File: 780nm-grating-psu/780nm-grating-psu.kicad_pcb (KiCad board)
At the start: 2 copper layers, 92.1 x 48.3 mm, 104 parts, among them IC1 ADP7142ARDZ-5.0-R7, IC2 LT8618EDDB#TRPBF, J1 TSW-102-07-G-D, J2 1755736, J3 54-00166, J4 TSW-102-07-G-S, J7 1715747, Q1 FDD3N40TM, Q2 2N7002, Q3 2N7002, U1 LT3757AEDD, U2 ADP7142ARDZ-3.3

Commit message: finished part placement
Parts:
- added REF**: Symbol_HighVoltage_Triangle_6x6mm_Copper, Symbol:Symbol_HighVoltage_Triangle_6x6mm_Copper, F.Cu at (191.0, 55.3)
- added SYM: Caution_Hot_Surface_FinalFit_12x12mm_Silk, caution:Caution_Hot_Surface_FinalFit_12x12mm_Silk, F.Cu at (207.3, 70.9)
- +155V TEST: renamed from TP8
- C11, C12: value 4.7u -> 2.2u; footprint Capacitor_SMD:C_0603_1608Metric -> Capacitor_SMD:C_2220_5750Metric
- moved +155V TEST 113.0 mm to (211.7, 48.7)
- moved Q1 101.2 mm to (222.2, 57.9), turned to 90 degrees
- moved R11 98.7 mm to (213.5, 64.7), turned to 180 degrees
- moved R10 97.2 mm to (215.0, 60.8), turned to -90 degrees
- moved R9 97.2 mm to (215.0, 55.8), turned to -90 degrees
- moved D2 93.6 mm to (238.1, 75.7)
- moved D1 91.5 mm to (228.2, 49.5), turned to -90 degrees
- moved R8 90.7 mm to (217.5, 51.4), turned to 180 degrees
- moved R7 85.1 mm to (222.7, 51.4), turned to 180 degrees
- moved J2 83.9 mm to (204.1, 39.0), turned to 180 degrees
- moved R20 82.2 mm to (238.0, 42.5), turned to 180 degrees
- moved R33 82.1 mm to (235.7, 67.7), turned to 180 degrees
- moved C31 81.8 mm to (219.0, 41.7), turned to 90 degrees
- moved R12 81.7 mm to (232.6, 46.8)
- moved R19 81.0 mm to (238.0, 45.0)
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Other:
- board size 92.1 x 48.3 mm -> 101 x 58 mm
- copper layers 2 -> 4
- board text added: "+155V PWR STATUS"
- board text added: "CAUTION HIGH VOLTAGE"
- board text added: "DNP"
- board text added: "GPIO INPUT"

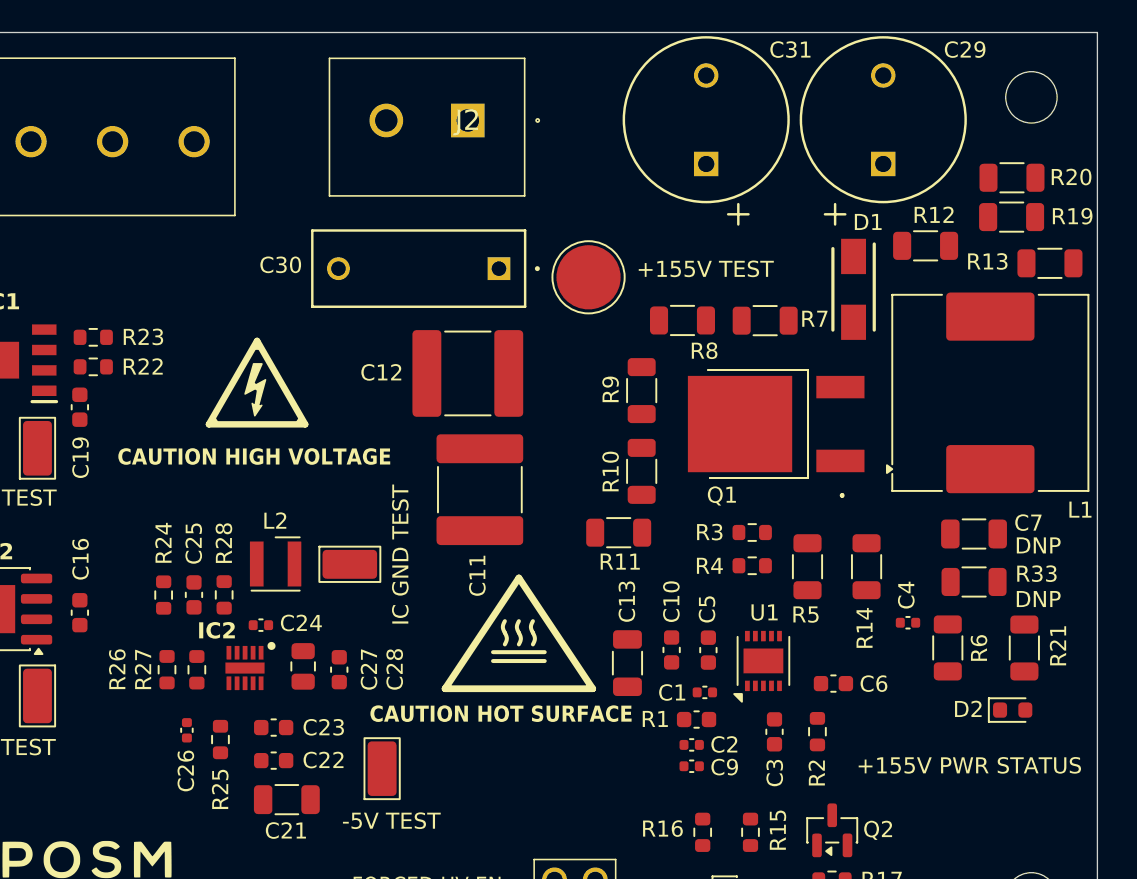
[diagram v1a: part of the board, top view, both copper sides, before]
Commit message: fixed hot loop
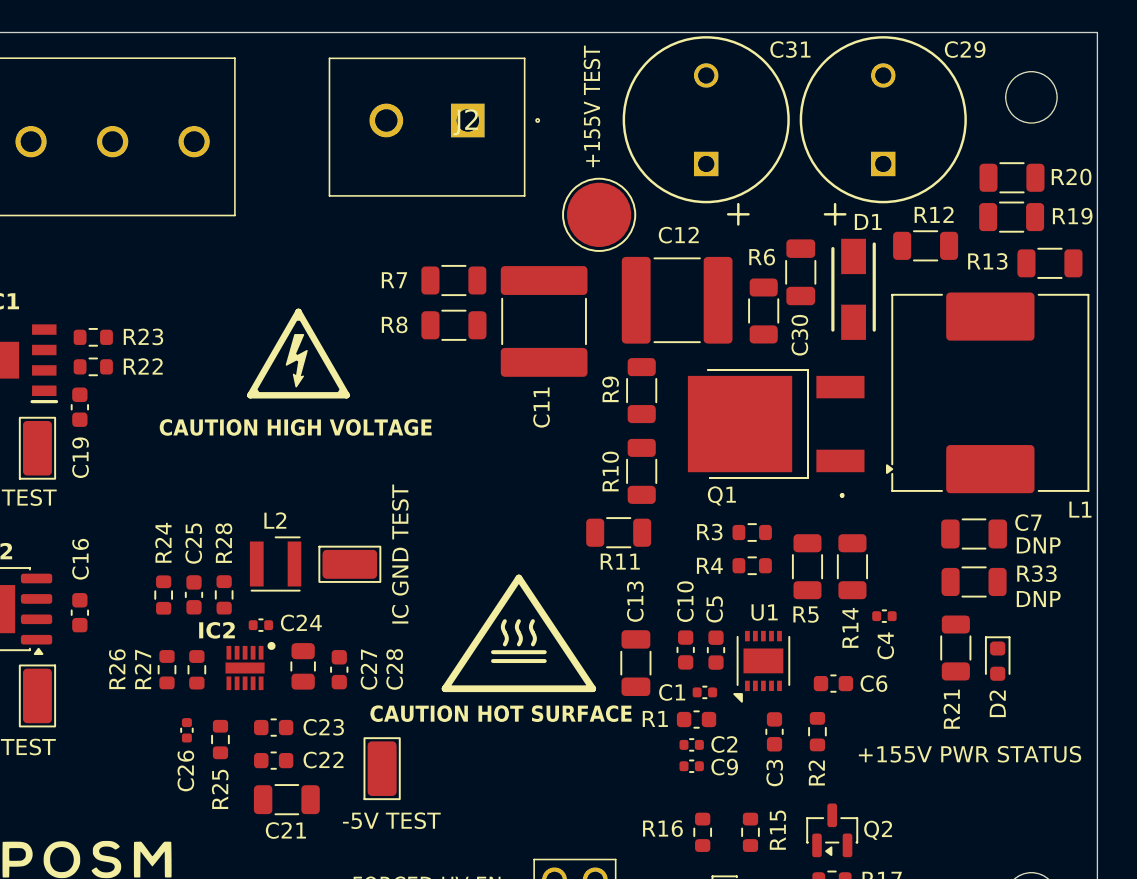
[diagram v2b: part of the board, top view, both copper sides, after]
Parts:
- C30: footprint PHE426HA6100JR05:CAP_PHE426_AH_KEM -> Capacitor_SMD:C_1206_3216Metric
- moved R6 23.9 mm to (222.6, 50.8), turned to -90 degrees
- moved R7 19.6 mm to (203.3, 48.9)
- moved C30 18.8 mm to (224.9, 48.4), turned to -90 degrees
- moved R8 14.2 mm to (203.3, 51.7), turned to 0 degrees
- moved C12 13.8 mm to (217.2, 50.2)
- moved C11 11.2 mm to (208.9, 51.5)
- moved R21 4.27 mm to (234.5, 71.8)
- moved +155V TEST 3.95 mm to (212.3, 44.9)
- moved D2 3.19 mm to (237.1, 72.7), turned to -90 degrees
- moved REF** 3.15 mm to (193.6, 53.5)
- moved C4 1.53 mm to (230.1, 69.8)
- moved R14 0.88 mm to (228.1, 66.8)
- moved C10 0.88 mm to (217.7, 72.0)
- moved C13 0.53 mm to (214.6, 72.8)
- moved C5 0.47 mm to (219.6, 72.0)
